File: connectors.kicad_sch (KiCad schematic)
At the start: 34 parts, among them J301 CONN_SMA_VERT, J302 CONN2, J303 CONN_SMA_VERT, J304 CONN3, J305 CONN_SMA_VERT, J306 CONN3, J307 CONN2, J308 CONN_SMA_VERT, J309 CONN8, Q301 BSS138

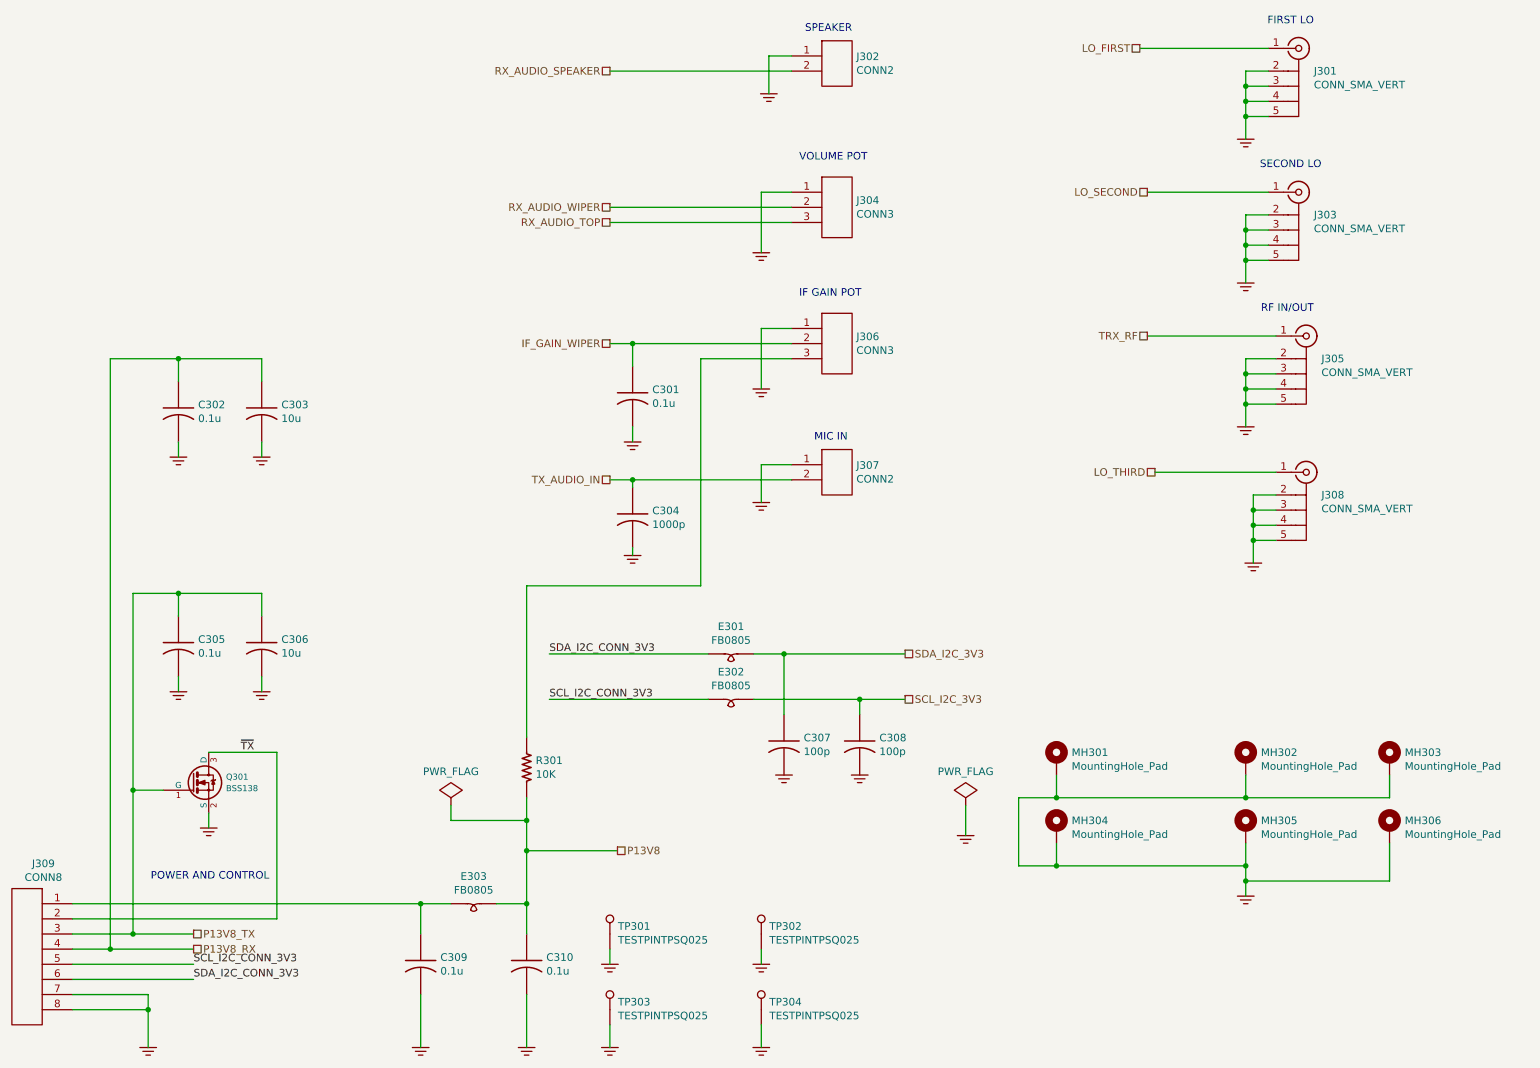
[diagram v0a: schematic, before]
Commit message: Update pcb database to version 6
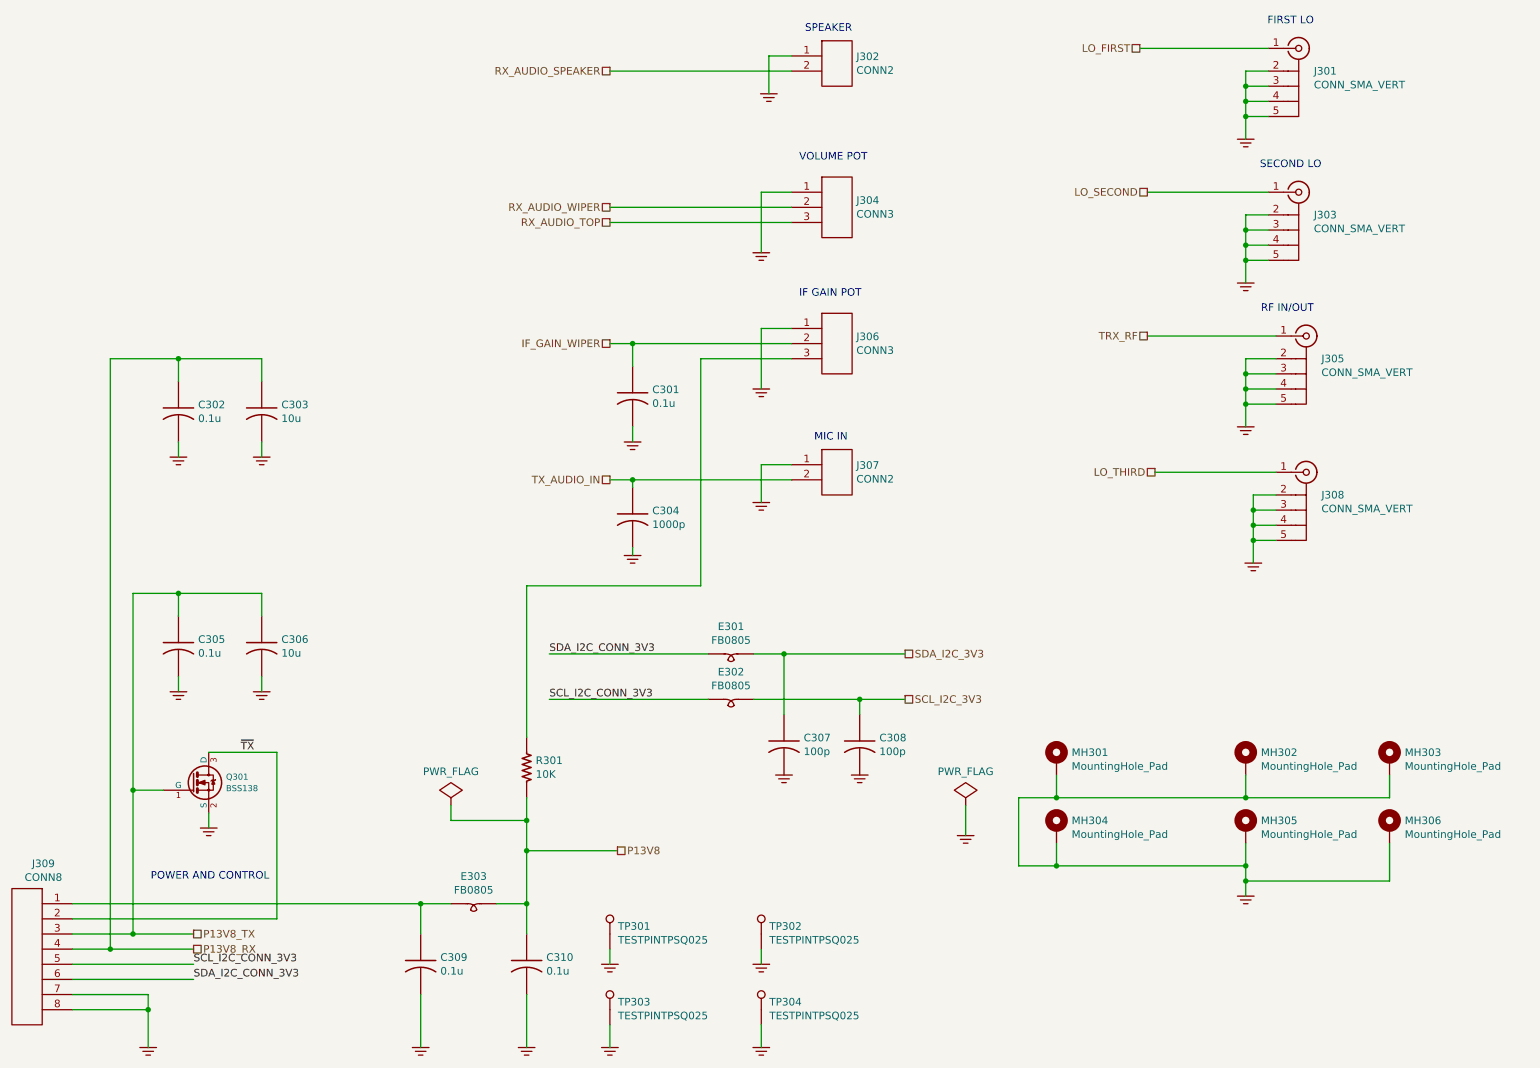
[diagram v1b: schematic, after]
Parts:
- C301, C302, C305, C309, C310: symbol Custom:C_US_0805_0.1UF_X7R_10%_50V_HS -> custom:C_US_0805_0.1UF_X7R_10%_50V_HS
- C303, C306: symbol Custom:C_US_0805_0.1UF_X7R_10%_50V_HS -> custom:C_US_0805_0.1UF_X7R_10%_50V_HS; PartNumber 800003-106 -> 800238-104
- C304: symbol Custom:C_US_0805_C0G_NPO_5%_50V_HS -> custom:C_US_0805_C0G_NPO_5%_50V_HS; PartNumber 800239-102 -> 800239_XXX
- C307, C308: symbol Custom:C_US_0805_C0G_NPO_5%_50V_HS -> custom:C_US_0805_C0G_NPO_5%_50V_HS; PartNumber 800239-101 -> 800239_XXX
- E301, E302, E303: symbol Custom:FB0805 -> custom:FB0805; PartNumber 800245-601 -> 80000X-XXX
- J301, J303, J305, J308: symbol Custom:CONN_SMA_VERT -> custom:CONN_SMA_VERT; PartNumber 800253-101 -> 800XXX-101
- J302, J307: symbol Custom:CONN2 -> custom:CONN2
- J304, J306: symbol Custom:CONN3 -> custom:CONN3
- J309: symbol Custom:CONN8 -> custom:CONN8
- Q301: symbol Custom:BSS138 -> custom:BSS138
- R301: symbol Custom:R_US_0805_1%_HS -> custom:R_US_0805_1%_HS; PartNumber 800235-103 -> 800235-XXX
- TP301, TP302, TP303, TP304: symbol Custom:TESTPINTPSQ025 -> custom:TESTPINTPSQ025

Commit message: Fix BOM part number errors and out of sync footprints which happened during conversion from Kicad 5 to 6
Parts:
- C303, C306: PartNumber 800238-104 -> 800003-106
- C304: PartNumber 800239_XXX -> 800239-103
- C307, C308: PartNumber 800239_XXX -> 800239-101
- E301, E302, E303: PartNumber 80000X-XXX -> 800245-601
- J301, J303, J305, J308: PartNumber 800XXX-101 -> 800253-101
- R301: PartNumber 800235-XXX -> 800235-103
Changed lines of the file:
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@@
       (effects (font (size 1.27 1.27)) hide)
     )
-    (property "PartNumber" "800XXX-101" (id 4) (at 229.87 26.67 0)
+    (property "PartNumber" "800253-101" (id 4) (at 229.87 26.67 0)
       (effects (font (size 1.27 1.27)) hide)
     )
@@
       (effects (font (size 1.27 1.27)) hide)
     )
-    (property "PartNumber" "800XXX-101" (id 4) (at 229.87 50.8 0)
+    (property "PartNumber" "800253-101" (id 4) (at 229.87 50.8 0)
       (effects (font (size 1.27 1.27)) hide)
     )
@@
       (effects (font (size 1.27 1.27)) hide)
     )
-    (property "PartNumber" "800XXX-101" (id 4) (at 231.14 74.93 0)
+    (property "PartNumber" "800253-101" (id 4) (at 231.14 74.93 0)
       (effects (font (size 1.27 1.27)) hide)
     )
@@
       (effects (font (size 1.524 1.524)))
     )
-    (property "PartNumber" "80000X-XXX" (id 4) (at 90.805 164.465 0)
+    (property "PartNumber" "800245-601" (id 4) (at 90.805 164.465 0)
       (effects (font (size 1.524 1.524)) hide)
     )
@@
       (effects (font (size 1.524 1.524)))
     )
-    (property "PartNumber" "800235-XXX" (id 4) (at 95.758 149.86 90)
+    (property "PartNumber" "800235-103" (id 4) (at 95.758 149.86 90)
       (effects (font (size 1.524 1.524)) hide)
     )
@@
       (effects (font (size 1.524 1.524)))
     )
-    (property "PartNumber" "800239_XXX" (id 4) (at 118.11 91.44 0)
+    (property "PartNumber" "800239-103" (id 4) (at 118.11 91.44 0)
       (effects (font (size 1.524 1.524)) hide)
     )
@@
       (effects (font (size 1.524 1.524)))
     )
-    (property "PartNumber" "800238-104" (id 4) (at 55.88 113.03 0)
+    (property "PartNumber" "800003-106" (id 4) (at 55.88 113.03 0)
       (effects (font (size 1.524 1.524)) hide)
     )
@@
       (effects (font (size 1.524 1.524)))
     )
-    (property "PartNumber" "80000X-XXX" (id 4) (at 133.985 122.555 0)
+    (property "PartNumber" "800245-601" (id 4) (at 133.985 122.555 0)
       (effects (font (size 1.524 1.524)) hide)
     )
@@
       (effects (font (size 1.524 1.524)))
     )
-    (property "PartNumber" "80000X-XXX" (id 4) (at 133.985 130.175 0)
+    (property "PartNumber" "800245-601" (id 4) (at 133.985 130.175 0)
       (effects (font (size 1.524 1.524)) hide)
     )
@@
       (effects (font (size 1.524 1.524)))
     )
-    (property "PartNumber" "800239_XXX" (id 4) (at 143.51 129.54 0)
+    (property "PartNumber" "800239-101" (id 4) (at 143.51 129.54 0)
       (effects (font (size 1.524 1.524)) hide)
     )
@@
       (effects (font (size 1.524 1.524)))
     )
-    (property "PartNumber" "800238-104" (id 4) (at 55.88 73.66 0)
+    (property "PartNumber" "800003-106" (id 4) (at 55.88 73.66 0)
       (effects (font (size 1.524 1.524)) hide)
     )
@@
       (effects (font (size 1.524 1.524)))
     )
-    (property "PartNumber" "800239_XXX" (id 4) (at 156.21 129.54 0)
+    (property "PartNumber" "800239-101" (id 4) (at 156.21 129.54 0)
       (effects (font (size 1.524 1.524)) hide)
     )
@@
       (effects (font (size 1.27 1.27)) hide)
     )
-    (property "PartNumber" "800XXX-101" (id 4) (at 231.14 97.79 0)
-      (effects (font (size 1.27 1.27)) hide)
-    )
+    (property "PartNumber" "800253-101" (id 4) (at 231.14 97.79 0)
+      (effects (font (size 1.27 1.27)) hide)
+    )
